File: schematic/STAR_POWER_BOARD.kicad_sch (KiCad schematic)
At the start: 62 parts, among them J1 1017491, J2 6120XX21621_61200621621, J3 1017491, J4 6120XX21621_61200621621, J5 6120XX21621_61200821621, Q1 CSD18540Q5B, Q2 CSD17577Q3A, Q3 CSD17577Q3A, Q4 CSD18540Q5B, U1 TPS566238PRQFR, U2 TPS566238PRQFR, U3 TPS40305DRCT

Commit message: POWER BOARD is ready for PCB to be made for the usb-c integration
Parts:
- added C34, C38, C41, C47, C48, C91, C94: 100n, Capacitor_SMD:C_0603_1608Metric_Pad1.08x0.95mm_HandSolder, symbol Device:C
- added C35: 1u, Capacitor_SMD:C_0603_1608Metric_Pad1.08x0.95mm_HandSolder, symbol Device:C
- added C36, C37, C39, C40, C42, C43, C44, C45, C46, C92, C95: 10u, Capacitor_SMD:C_0805_2012Metric_Pad1.18x1.45mm_HandSolder, symbol Device:C
- added C49, C51: 4u7, Capacitor_SMD:C_0805_2012Metric_Pad1.18x1.45mm_HandSolder, symbol Device:C
- added C50, C90: 330p, Capacitor_SMD:C_0603_1608Metric_Pad1.08x0.95mm_HandSolder, symbol Device:C
- added C52, C53, C88, C89: 10n, Capacitor_SMD:C_0603_1608Metric_Pad1.08x0.95mm_HandSolder, symbol Device:C
- added C93: 22u, T527T226M025ATE100:CAPPM3528X120N, symbol Device:C_Polarized
- added D5, D6: 82306050029, 82306050029:WESURGE_0603134, symbol 82306050029:82306050029
- added FB2: 22R, Resistor_SMD:R_0603_1608Metric_Pad0.98x0.95mm_HandSolder, symbol Device:FerriteBead_Small
- added J7: PD_DBG, Connector_PinHeader_2.54mm:PinHeader_1x03_P2.54mm_Vertical, symbol Connector_Generic:Conn_01x03
- added J8: PD_I2C, Connector_PinHeader_2.54mm:PinHeader_1x04_P2.54mm_Vertical, symbol Connector_Generic:Conn_01x04
- added J9: USB4216-03-A, USB421603A, symbol USB4216-03-A:USB4216-03-A
- added R11, R12, R13, R14: 10k, Resistor_SMD:R_0603_1608Metric_Pad0.98x0.95mm_HandSolder, symbol Device:R
- added R15, R24: 3k3, Resistor_SMD:R_0603_1608Metric_Pad0.98x0.95mm_HandSolder, symbol Device:R
- added U4: CAT24C512WI-GT3, CAT24C512WI-GT3:SOIC127P600X175-8N, symbol CAT24C512WI:CAT24C512WI-GT3
- added U8: TPS25751DREFR, TPS25751DREFR:TPS25751DREFR, symbol TPS25751DREFR:TPS25751DREFR
- added U9: TVS2200DRV, TVS2200DRVR:SON65P200X200X80-7N, symbol Power_Protection:TVS2200DRV
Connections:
- net GND: now also C34.2, C35.2, C36.2, C37.2, C38.2, C39.2, C40.2, C41.2, C42.2, C43.2, C44.2, C45.2, C46.2, C47.2, C48.2, C49.2, C50.2, C51.2, C52.1, C53.1, C88.1, C89.1, C90.2, C91.2, C92.2, C93.2, C94.2, C95.2, D5.2 (A2), D6.2 (A2), J7.1 (Pin_1), J8.1 (Pin_1), J9.A1 (GND_1), J9.B1 (GND_2), J9.G1 (GND_3), J9.G2 (GND_4), J9.G3 (GND_5), J9.G4 (GND_6), R11.1, R12.1, R13.1, R14.1, U4.4 (VSS), U8.10 (~{I2CT_IRQ}), U8.11 (GND_1), U8.12 (GND_2), U8.13 (GPIO11), U8.14 (GND_3), U8.18 (~{I2CC_IRQ}), U8.19 (GPIO3), U8.2 (ADCIN1), U8.3 (ADCIN2), U8.31 (GND_4), U8.36 (GPIO7), U8.37 (GPIO6), U8.39 (GND_5), U8.5 (GPIO0), U8.6 (GPIO1), U8.7 (GPIO2), U9.1 (GND), U9.2 (GND), U9.3 (GND), U9.7 (GND)
- net P3V3_BUCK: now also C94.1, C95.1, U8.38 (VIN_3V3)
- net P5V0_BUCK: now also C42.1, C43.1, C44.1, C45.1, C46.1, C47.1, C91.1, C92.1, C93.1, U8.20 (PPHV), U8.21 (PPHV), U8.22 (PPHV), U8.34 (PP5V), U8.35 (PP5V)
- net SYS_VOLTAGE renamed PACK+
- new net: R11.2, U4.1 (A0)
- new net: R12.2, U4.2 (A1)
- new net: R13.2, U4.3 (A2)
- new net: R14.2, U4.7 (WP)
- new net: C52.2, C53.2, C88.2, C89.2, FB2.1, J9.A4 (VBUS_1), J9.B4 (VBUS_2), U9.4 (IN), U9.5 (IN), U9.6 (IN)
- new net: C39.1, C40.1, C41.1, U8.4 (LDO_1V5)
- new net: J8.3 (Pin_3), U8.8 (I2CT_SDA)
- new net: J8.2 (Pin_2), U8.9 (I2CT_SCL)
- new net C_CC1: C50.1, J9.A5 (CC1), U8.28 (CC1)
- new net C_CC2: C90.1, J9.B5 (CC2), U8.29 (CC2)
- new net USBC_DRAIN: U8.15 (DRAIN_1), U8.30 (DRAIN_2), U8.40 (DRAIN_3)
- new net USBC_LDO_3V3: C34.1, C35.1, C36.1, C37.1, C38.1, J8.4 (Pin_4), R15.2, R24.2, U4.8 (VCC), U8.1 (LDO_3V3)
- new net USBC_N: D6.1 (A1), J9.A7 (DN1), J9.B7 (DN2), U8.27 (GPIO5/USB_N/LD2)
- new net USBC_P: D5.1 (A1), J9.A6 (DP1), J9.B6 (DP2), U8.26 (GPIO4/USB_P/LD1)
- new net USBC_SCL: J7.2 (Pin_2), R24.1, U4.6 (SCL), U8.17 (I2CC_SCL)
- new net USBC_SDA: J7.3 (Pin_3), R15.1, U4.5 (SDA), U8.16 (I2CC_SDA)
- new net USBC_VBUS: C48.1, C49.1, C51.1, FB2.2, U8.23 (VBUS_IN), U8.24 (VBUS_IN), U8.25 (VBUS_IN), U8.32 (VBUS), U8.33 (VBUS)
- no-connect marks 4 -> 6
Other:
- note added: ""can be used to directly program the TPS25751, and program the BQ25798 through the host microcontroller " ^^^^ for the I2Ct lines (pins 8, 9)"
- note added: "** Override, PPHV to be 5V0 Buck **"
- note added: "1010 ???? GND=0 so this: 1010 0000 -> 0x50 which is what we need for our PD controller"
- note added: "512Kb"
- note added: "ADCIN1 & ADCIN2 configured for "SafeMode" I2C Target is 0x21"
- note added: "EEPROM"
- note added: "Flash this with the bin taken from TI's website. Use I2C to USB adapter. Flash this when the system is off (not powered), only flash/power this."
- note added: "PACK+"
- note added: "TPS25751DREFR will load from EEPROM"
- note added: "USB-C"
- note added: "USB-C PD Controller"
- note added: "internal debugging"
- note added: "pins 15&30 tie to exposed pad 40 for internal fet"
- note removed: "SYS"
- moved on the sheet: H1, H2, H3, H4, J1, J2, J3, J4, J5

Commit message: done lil bro
done lil bro
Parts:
- removed C34, C38, C41, C47, C48, C91, C94: 100n, Capacitor_SMD:C_0603_1608Metric_Pad1.08x0.95mm_HandSolder, symbol Device:C
- removed C35: 1u, Capacitor_SMD:C_0603_1608Metric_Pad1.08x0.95mm_HandSolder, symbol Device:C
- removed C36, C37, C39, C40, C42, C43, C44, C45, C46, C92, C95: 10u, Capacitor_SMD:C_0805_2012Metric_Pad1.18x1.45mm_HandSolder, symbol Device:C
- removed C49, C51: 4u7, Capacitor_SMD:C_0805_2012Metric_Pad1.18x1.45mm_HandSolder, symbol Device:C
- removed C50, C90: 330p, Capacitor_SMD:C_0603_1608Metric_Pad1.08x0.95mm_HandSolder, symbol Device:C
- removed C52, C53, C88, C89: 10n, Capacitor_SMD:C_0603_1608Metric_Pad1.08x0.95mm_HandSolder, symbol Device:C
- removed C93: 22u, T527T226M025ATE100:CAPPM3528X120N, symbol Device:C_Polarized
- removed D5, D6: 82306050029, 82306050029:WESURGE_0603134, symbol 82306050029:82306050029
- removed FB2: 22R, Resistor_SMD:R_0603_1608Metric_Pad0.98x0.95mm_HandSolder, symbol Device:FerriteBead_Small
- removed J7: PD_DBG, Connector_PinHeader_2.54mm:PinHeader_1x03_P2.54mm_Vertical, symbol Connector_Generic:Conn_01x03
- removed J8: PD_I2C, Connector_PinHeader_2.54mm:PinHeader_1x04_P2.54mm_Vertical, symbol Connector_Generic:Conn_01x04
- removed R11, R14: 10k, Resistor_SMD:R_0603_1608Metric_Pad0.98x0.95mm_HandSolder, symbol Device:R
- removed R15, R24: 3k3, Resistor_SMD:R_0603_1608Metric_Pad0.98x0.95mm_HandSolder, symbol Device:R
- removed U4: CAT24C512WI-GT3, CAT24C512WI-GT3:SOIC127P600X175-8N, symbol CAT24C512WI:CAT24C512WI-GT3
- removed U8: TPS25751DREFR, TPS25751DREFR:TPS25751DREFR, symbol TPS25751DREFR:TPS25751DREFR
- removed U9: TVS2200DRV, TVS2200DRVR:SON65P200X200X80-7N, symbol Power_Protection:TVS2200DRV
- added Q5: SSM6J507NU-LF, SSM6J507NULF, symbol SSM6J507NU-LF:SSM6J507NU-LF
- R12, R13: DigiKey Link https://www.digikey.com/short/2f9q7213 -> https://www.digikey.com/short/tv9hzj27; DigiKey Part Number YAG2313CT-ND -> P10KDBCT-ND; DigiKey Price per Unit 0.14 -> 0.10; Manufactaurer Part Number (none) -> CRCW0603220KFKEA; Manufacturer Part Number RT0603BRE0710KL -> (none); Manufacturer_Part_Number (none) -> ERA-3AEB103V; Mouser Link https://mou.sr/3VPcUDd -> https://mou.sr/4g4GMTT; Mouser Part Number 603-RT0603BRE0710KL -> 667-ERA-3AEB103V
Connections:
- net C_CC1 is gone; now on an unnamed net: J9.A5 (CC1)
- net C_CC2 is gone; now on an unnamed net: J9.B5 (CC2)
- net GND: now also Q5.3; no longer R12.1, R13.1
- net P5V0_BUCK: now also R12.1, R13.1, Q5.1, Q5.2 (D), Q5.5 (D), Q5.6 (D), Q5.7 (D)
- net USBC_VBUS: now also J9.A4 (VBUS_1), J9.B4 (VBUS_2), Q5.4, Q5.8 (S)
- net USBC_N: no longer names the net of J9.A7 (DN1)
- net USBC_N: no longer J9.B7 (DN2)
- net USBC_P: no longer names the net of J9.A6 (DP1)
- net USBC_P: no longer J9.B6 (DP2)
- no-connect marks 6 -> 10
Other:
- note removed: ""can be used to directly program the TPS25751, and program the BQ25798 through the host microcontroller " ^^^^ for the I2Ct lines (pins 8, 9)"
- note removed: "** Override, PPHV to be 5V0 Buck **"
- note removed: "1010 ???? GND=0 so this: 1010 0000 -> 0x50 which is what we need for our PD controller"
- note removed: "512Kb"
- note removed: "ADCIN1 & ADCIN2 configured for "SafeMode" I2C Target is 0x21"
- note removed: "EEPROM"
- note removed: "Flash this with the bin taken from TI's website. Use I2C to USB adapter. Flash this when the system is off (not powered), only flash/power this."
- note removed: "TPS25751DREFR will load from EEPROM"
- note removed: "USB-C PD Controller"
- note removed: "internal debugging"
- note removed: "pins 15&30 tie to exposed pad 40 for internal fet"
- moved on the sheet: J9

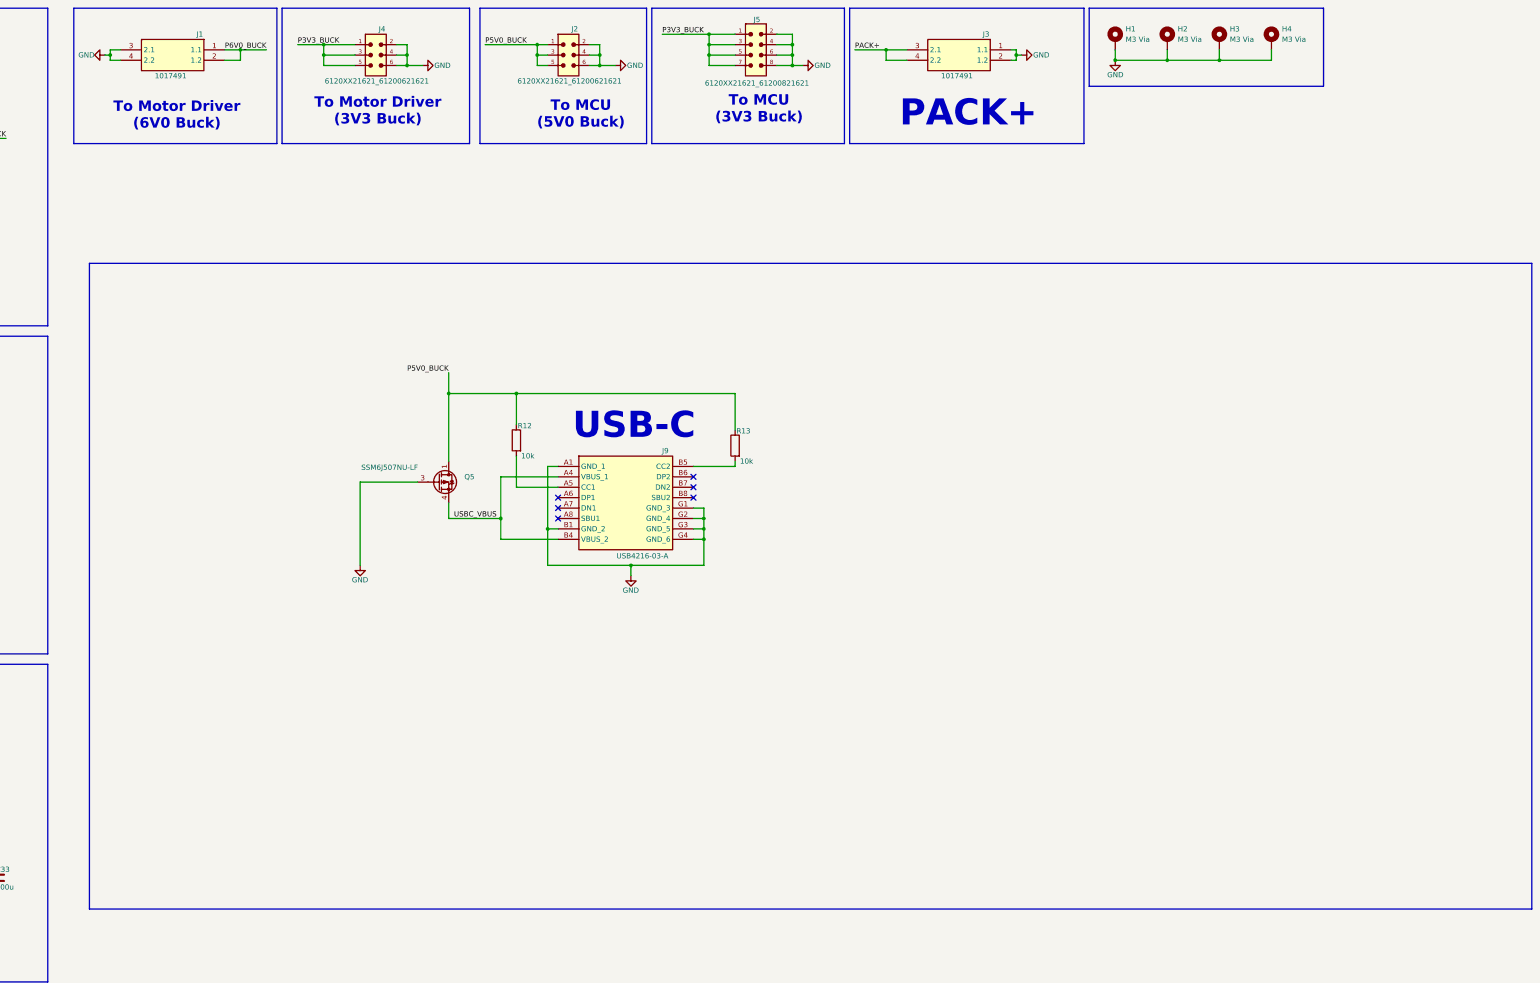
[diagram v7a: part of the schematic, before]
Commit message: Finished Power Board, working on BMS, moved Motor Driver to archive, added Motor Driver to MCU
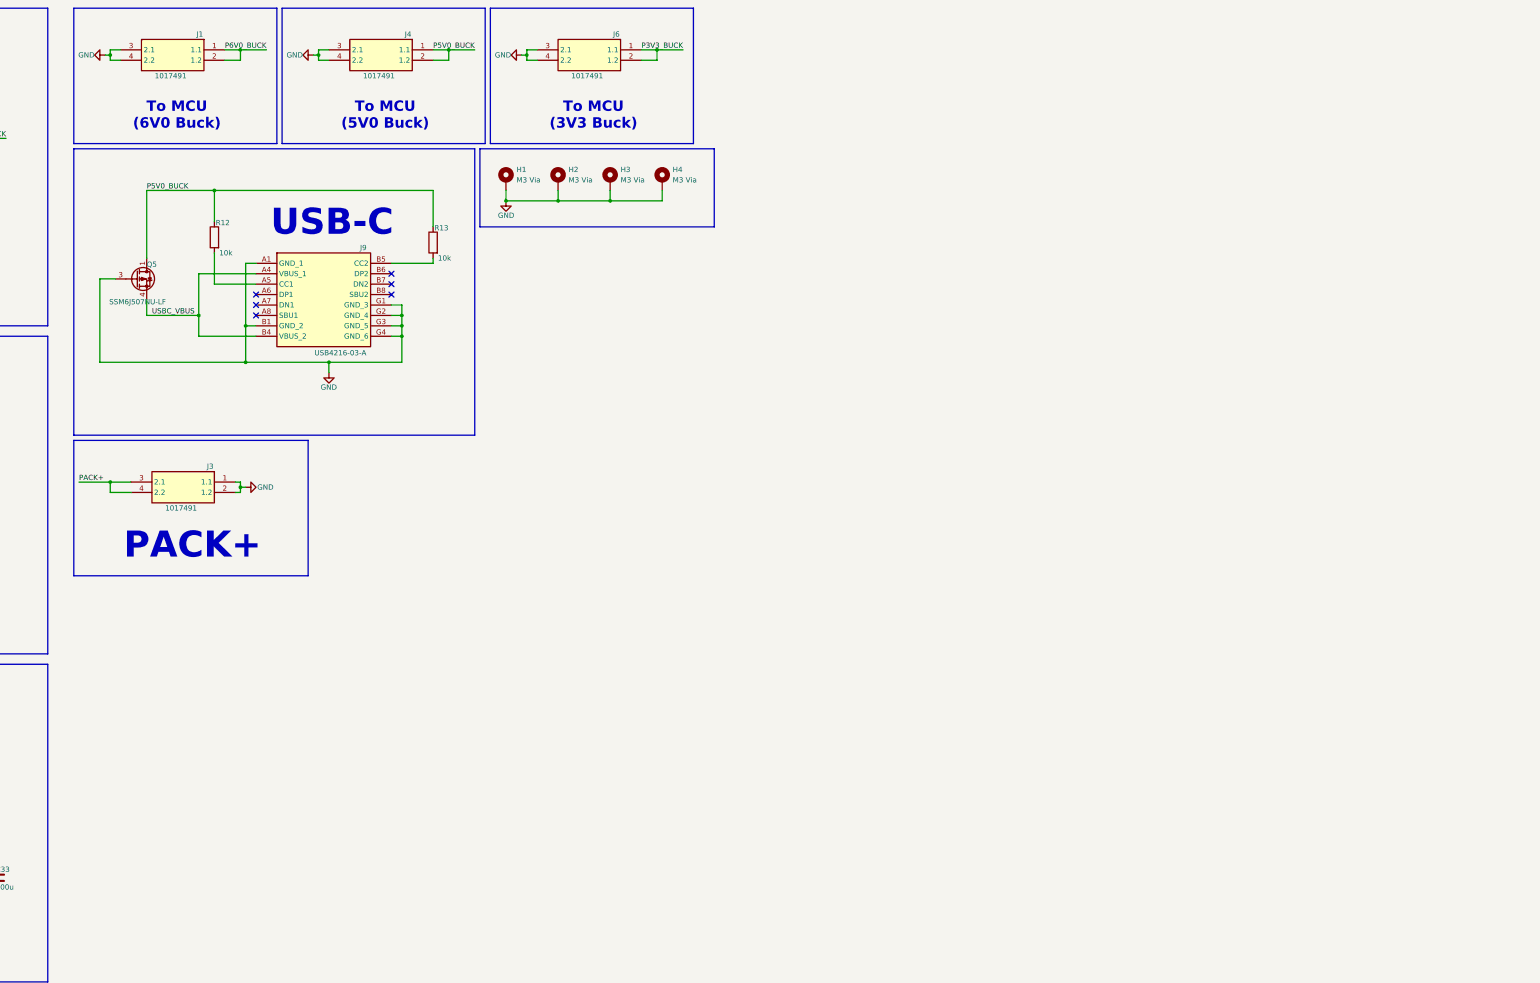
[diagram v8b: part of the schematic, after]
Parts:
- removed J2, J4: 6120XX21621_61200621621, 61200621621:61200621621, symbol 61200621621:6120XX21621_61200621621
- removed J5: 6120XX21621_61200821621, 61200821621:61200821621, symbol 61200821621:6120XX21621_61200821621
- added J4, J6: 1017491, 1017491, symbol 1017491:1017491
- C1, C4, C7: DigiKey Link N/A -> https://www.digikey.com/short/5wt33t20; DigiKey Part Number N/A -> 311-1779-1-ND; DigiKey Price per Unit N/A -> 0.10
- C10: Manufactaurer Part Number CC0603JRX7R9BB104 -> CL10B105KA8NNNC
- C14, C16: Manufactaurer Part Number 963-UMK107AB7105KA-T -> CL10B105KA8NNNC
- H1, H2, H3, H4: DigiKey Link (none) -> n/a; DigiKey Part Number (none) -> n/a; DigiKey Price per Unit (none) -> n/a; Manufactaurer Part Number (none) -> n/a; Mouser Link (none) -> n/a; Mouser Part Number (none) -> n/a; Mouser Price per Unit (none) -> n/a
- J1, J3: Manufactaurer Part Number (none) -> 1017491
- J9: Manufactaurer Part Number (none) -> USB4216-03-A
- L3: DigiKey Link n.a -> 118-SPB1308-R44MCT-ND; DigiKey Part Number n/a -> https://www.digikey.com/short/989z0w4f
- Q5: DigiKey Link (none) -> https://www.digikey.com/short/mhv57pnt; DigiKey Part Number (none) -> SSM6J507NULFCT-ND; DigiKey Price per Unit (none) -> 0.71; Manufactaurer Part Number (none) -> SSM6J507NU,LF; Mouser Link (none) -> https://mou.sr/3YaJUaq; Mouser Price per Unit (none) -> 0.73
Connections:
- net GND: now also J4.3 (2.1), J4.4 (2.2), J6.3 (2.1), J6.4 (2.2)
- net P3V3_BUCK: now also J6.1 (1.1), J6.2 (1.2)
- net P5V0_BUCK: now also J4.1 (1.1), J4.2 (1.2)
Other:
- note added: "To MCU (6V0 Buck)"
- note removed: "To Motor Driver (3V3 Buck)"
- note removed: "To Motor Driver (6V0 Buck)"
- moved on the sheet: H1, H2, H3, H4, J3, J9, Q5, R12, R13
